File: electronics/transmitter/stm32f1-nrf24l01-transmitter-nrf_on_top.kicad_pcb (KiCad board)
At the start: 2 copper layers, 86.4 x 35.6 mm, 24 parts, among them K1 CONN_3, K10 CONN_3, K11 CONN_3, K2 CONN_3, K3 CONN_3, K4 CONN_3, K5 CONN_3, K6 CONN_3, K7 CONN_3, K8 CONN_3, K9 CONN_3, P2 LED, Q1 BC548, SW1 ON/OFF, U1 LIPO_CHARGER_+_PROTECTION, U2 STM32F103C8T6_DEV_BOARD, U3 NRF24L01P

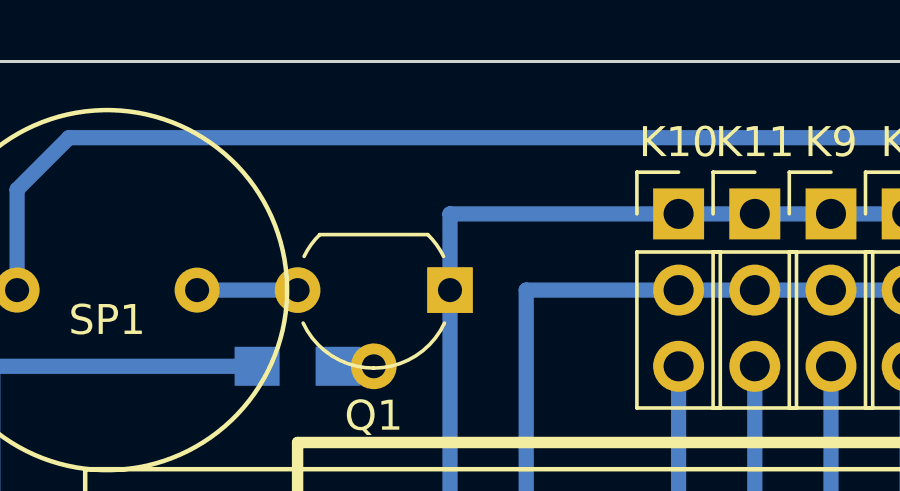
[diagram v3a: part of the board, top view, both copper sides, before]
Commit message: Add decoupling cap near buzzer
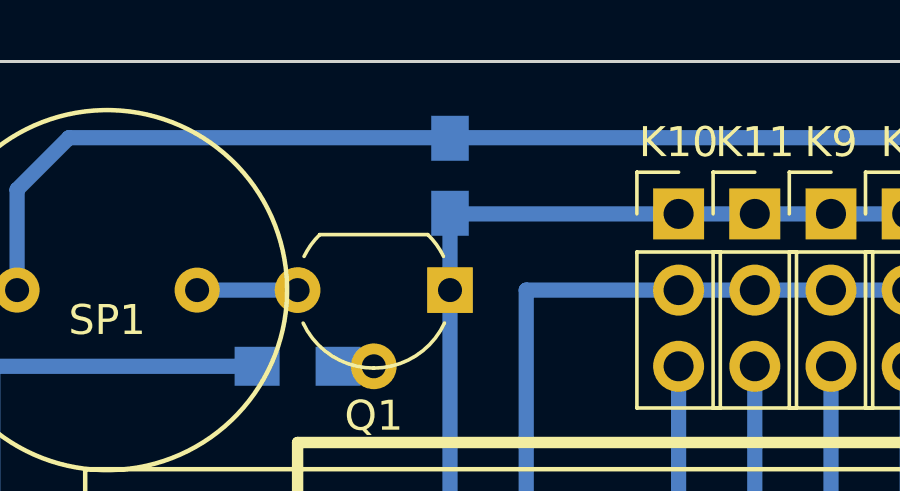
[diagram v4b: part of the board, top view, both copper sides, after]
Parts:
- added REF**: C_0805_HandSoldering, Capacitors_SMD:C_0805_HandSoldering, B.Cu at (228.6, 108.0)
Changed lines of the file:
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@@
 (kicad_pcb (version 4) (host pcbnew 4.0.5-e0-6337~49~ubuntu16.04.1)
   (general
-    (links 61)
+    (links 0)
     (no_connects 4)
     (area 210.769999 104.089999 297.230001 139.750001)
@@
     (tracks 103)
     (zones 0)
-    (modules 24)
+    (modules 25)
     (nets 46)
   )
@@
   )
   (setup
-    (last_trace_width 0.508)
+    (last_trace_width 0.254)
     (user_trace_width 0.508)
     (trace_clearance 0.1016)
@@
     (pad_to_mask_clearance 0)
     (aux_axis_origin 210.82 139.7)
-    (visible_elements 7FFFFF1F)
+    (visible_elements 7FFFFF3F)
     (pcbplotparams
       (layerselection 0x00030_80000001)
@@
       (at (xyz 0 0 0))
       (scale (xyz 1 1 1))
+      (rotate (xyz 0 0 0))
+    )
+  )
+  (module Capacitors_SMD:C_0805_HandSoldering (layer B.Cu)
+    (at 228.6 107.95 270)
+    (descr "Capacitor SMD 0805, hand soldering")
+    (tags "capacitor 0805")
+    (attr smd)
+    (fp_text reference REF** (at 0 2.1 270) (layer B.SilkS)
+      (effects (font (size 1 1) (thickness 0.15)) (justify mirror))
+    )
+    (fp_text value C_0805_HandSoldering (at 0 -2.1 270) (layer B.Fab)
+      (effects (font (size 1 1) (thickness 0.15)) (justify mirror))
+    )
+    (fp_line (start -1 -0.625) (end -1 0.625) (layer B.Fab) (width 0.1))
+    (fp_line (start 1 -0.625) (end -1 -0.625) (layer B.Fab) (width 0.1))
+    (fp_line (start 1 0.625) (end 1 -0.625) (layer B.Fab) (width 0.1))
+    (fp_line (start -1 0.625) (end 1 0.625) (layer B.Fab) (width 0.1))
+    (fp_line (start -2.3 1) (end 2.3 1) (layer B.CrtYd) (width 0.05))
+    (fp_line (start -2.3 -1) (end 2.3 -1) (layer B.CrtYd) (width 0.05))
+    (fp_line (start -2.3 1) (end -2.3 -1) (layer B.CrtYd) (width 0.05))
+    (fp_line (start 2.3 1) (end 2.3 -1) (layer B.CrtYd) (width 0.05))
+    (fp_line (start 0.5 0.85) (end -0.5 0.85) (layer B.SilkS) (width 0.12))
+    (fp_line (start -0.5 -0.85) (end 0.5 -0.85) (layer B.SilkS) (width 0.12))
+    (pad 1 smd rect (at -1.25 0 270) (size 1.5 1.25) (layers B.Cu B.Paste B.Mask))
+    (pad 2 smd rect (at 1.25 0 270) (size 1.5 1.25) (layers B.Cu B.Paste B.Mask))
+    (model Capacitors_SMD.3dshapes/C_0805_HandSoldering.wrl
+      (at (xyz 0 0 0))
+      (scale (xyz 1 1 1))

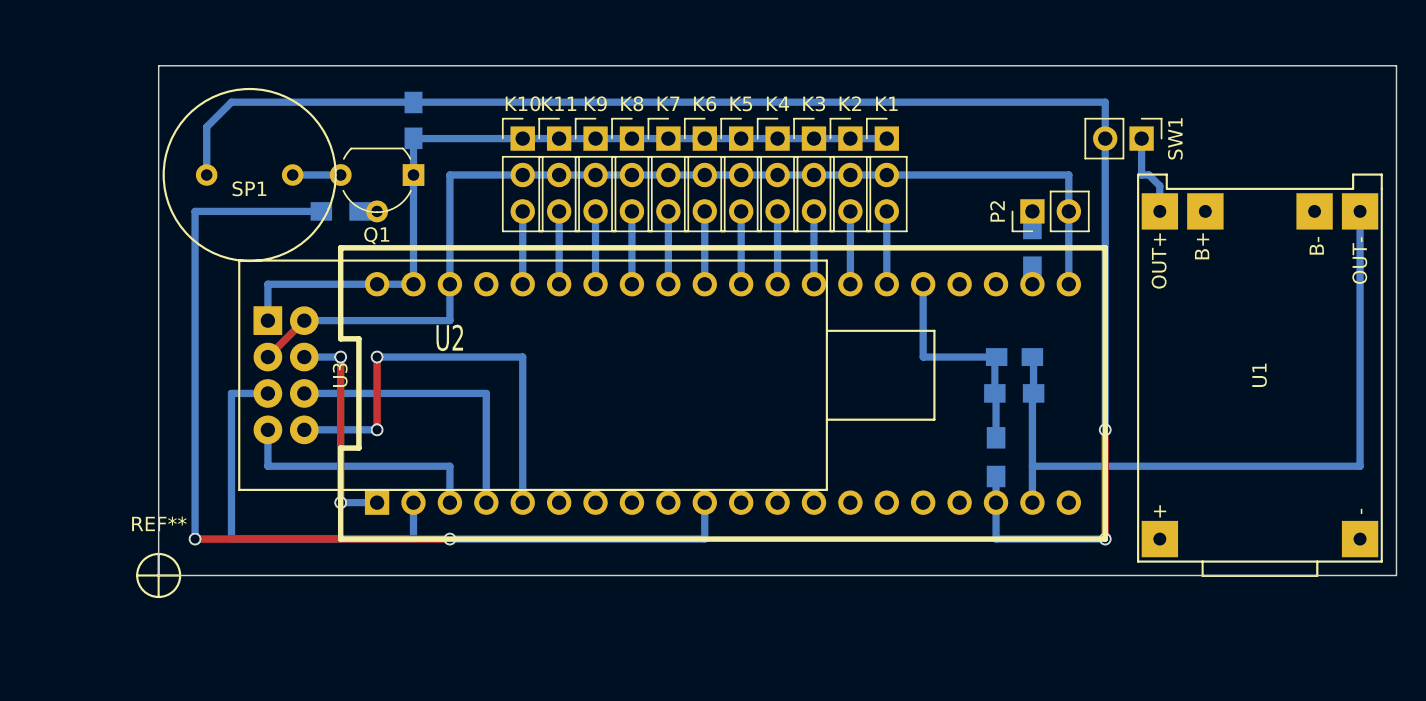
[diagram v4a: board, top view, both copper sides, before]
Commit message: Fix transistor footprint, add decoupling cap for buzzer, minor tweaks
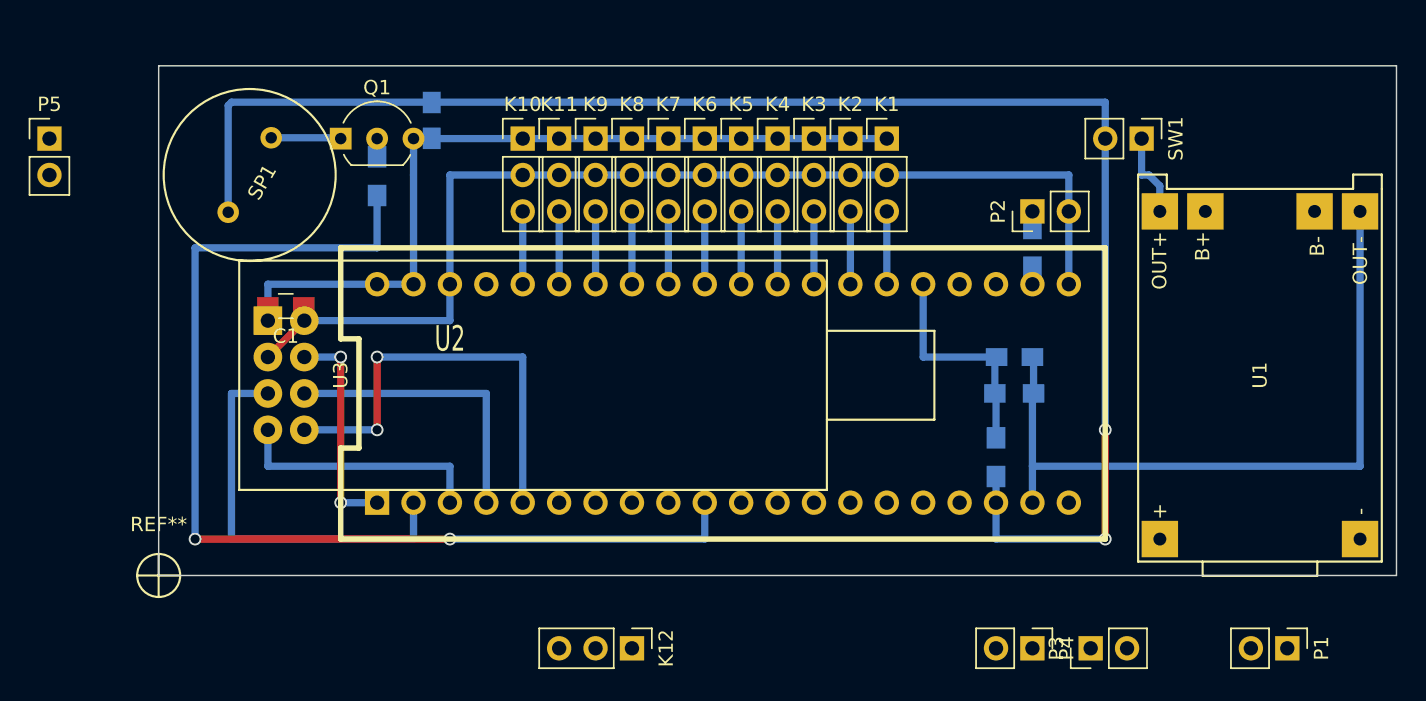
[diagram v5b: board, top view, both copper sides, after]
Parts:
- removed the REF** at (228.6, 108.0)
- added C1: 1u, Capacitors_SMD:C_0805_HandSoldering, F.Cu at (219.7, 120.9)
- added C3: 1u, Capacitors_SMD:C_0805_HandSoldering, B.Cu at (229.9, 108.0)
- added K12: UART, Pin_Headers:Pin_Header_Straight_1x03_Pitch2.54mm, F.Cu at (243.8, 144.8)
- added P1: Charge, Pin_Headers:Pin_Header_Straight_1x02_Pitch2.54mm, F.Cu at (289.6, 144.8)
- added P3: PWR-BAT, Pin_Headers:Pin_Header_Straight_1x02_Pitch2.54mm, F.Cu at (275.8, 144.8)
- added P4: PWR-IN, Pin_Headers:Pin_Header_Straight_1x02_Pitch2.54mm, F.Cu at (271.8, 144.8)
- added P5: Buzzer, Pin_Headers:Pin_Header_Straight_1x02_Pitch2.54mm, F.Cu at (203.2, 109.2)
- Q1: value BC548 -> BC547B; footprint TO_SOT_Packages_THT:TO-92_Molded_Wide -> TO_SOT_Packages_THT:TO-92_Inline_Wide
- moved Q1 5.68 mm to (223.5, 109.2), turned to 0 degrees
- moved R4 3.54 mm to (226.1, 111.8), turned to 90 degrees
- turned SP1 to 60 degrees
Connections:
- Q1 pad 1: GND -> Net-(P5-Pad1)
- Q1 pad 3: Net-(P5-Pad1) -> GND
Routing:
- net /BUZZER: track 69.8 -> 74.8 mm
- net VDD: track 109.6 -> 111.6 mm
- net Net-(P5-Pad1): track 3.35 -> 4.87 mm
